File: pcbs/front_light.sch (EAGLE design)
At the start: 13 parts, among them IC1 MC34063AD, J1 22-27-2041-04

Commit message: Front light: use attiny and LT3474
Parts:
- removed D2: SFH206, opto-trans-siemens:SFH206
- added ANODE1, CATHODE1: TPTP20SQ, testpad:TPTP20SQ
- added C10, C11, C14, C5: 100n, resistor:C-EUC0603
- added C13: 100u, resistor:CPOL-EUE
- added C3, C8: 220n, resistor:C-EUC0603
- added C4, C9: 3.3n, resistor:C-EUC0603
- added C6, C7: 2.2u, resistor:C-EUC0805
- added D3: LL5819, Brunner:DIODESCHOTTKY
- added H1: MOUNT-HOLE3.0, holes:MOUNT-HOLE3.0
- added IC2: LT3474, ltc_swr:LT3474
- added IC3: ATTINY24/44/84-SSU, attiny24_44_84:ATTINY24/44/84-SSU
- added J2: 22-27-2041-04, con-molex:22-27-2041-04
- added L2: DR74, inductors:DR74
- added LED1: (no value), led:LEDCHIPLED_0603
- added LIGHT, SPEED_SENSOR: 22-27-2021-02, con-molex:22-27-2021-02
- added LOGO1: OSHW_LOGO_6MILX0100-NT, ea:OSHW_LOGO_6MILX0100-NT
- added R10: 100k, resistor:R-EU_R0603
- added R11, R5: 10k, resistor:R-EU_R0603
- added R12, R6: 20k, resistor:R-EU_R0603
- added R13, R14: (no value), resistor:R-EU_R0603
- added R7, R8: 52.3k, resistor:R-EU_R0603
- added R9: 33, resistor:R-EU_R0603
- added U$1: TPS71530, ShortCircuitRobotics:TPS71530
- added U$2: ISP_SPECIALS, bookla:ISP_SPECIALS
- added U$4: IRF7103, irf-2:IRF7103
- C1: value 10u -> 2.2u; device resistor:C-EUC1206 -> resistor:C-EUC0805
- C2: value 330p -> 2.2u
- IC1: value MC34063AD -> LT3474; device v-reg-3:MC34063AD -> ltc_swr:LT3474
- J1: value 22-27-2041-04 -> (none); device con-molex:22-27-2041-04 -> con-amp:MTA02-156
- L1: value 470u -> DR74; device inductor-coilcraft:MSS1260 -> inductors:DR74
- R1: value 1R0 -> 52.3k; device rcl:R-EU_R1206 -> resistor:R-EU_R0603
- R2: value (none) -> 52.3k; device resistor:R-EU_R1206 -> resistor:R-EU_R0603
- R3: value 1R0 -> 33; device rcl:R-EU_R1206 -> resistor:R-EU_R0603
- R4: value 1R0 -> 100k; device rcl:R-EU_R1206 -> resistor:R-EU_R0603
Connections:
- removed net LED_A: ANODE.TP, IC1.IPK, R1.2, R3.2, R4.2
- removed net LED_C: CATHODE.TP, L1.P$1
- removed net LIGHT: D2.C, J1-3.S
- removed net PWM: IC1.COMP, J1-2.S, R2.2
- new net +12V: C1.1, C11.1, C13.+, C6.1, IC1G$1.#SHDN, IC1G$1.V_IN, IC2G$1.#SHDN, IC2G$1.V_IN, J1.1, U$1.VIN
- new net DI: IC3.(PCINT6/OC1A/SDA/MOSI/ADC6)PA6, J2-3.S, U$2.MOSI
- new net DO: IC3.(PCINT5/OC1B/MISO/DO/ADC5)PA5, J2-2.S, U$2.MISO
- new net N$10: R3.2, R4.2, U$4G$2.G
- new net N$11: IC1G$1.V_ADJ, R5.1, R6.2
- new net N$12: C8.2, D1.C, IC2G$1.SW, L1.1
- new net N$13: C7.1, IC2G$1.BIAS, IC2G$1.OUT, L1.2
- new net N$14: IC2G$1.RT, R7.2
- new net N$15: IC2G$1.REF, R11.1
- new net N$16: C8.1, IC2G$1.BOOST
- new net N$17: C9.1, IC2G$1.V_C, R8.2
- new net N$18: C10.1, R8.1
- new net N$19: ANODE1.TP, IC2G$1.LED
- new net N$2: C2.1, IC1G$1.BIAS, IC1G$1.OUT, L2.2
- new net N$20: CATHODE1.TP, U$4G$1.D@1, U$4G$1.D@2
- new net N$21: R10.2, R9.2, U$4G$1.G
- new net N$22: IC2G$1.V_ADJ, R11.2, R12.2
- new net N$23: IC3.(PCINT4/T1/SCL/USCK/ADC4)PA4, U$2.SCK
- new net N$24: IC3.(PCINT0/AREF/ADC0)PA0, LIGHT-1.S, R14.1
- new net N$25: IC3.(PCINT3/T0/ADC3)PA3, R13.1
- new net N$26: LED1.A, R13.2
- new net N$27: IC3.(PCINT1/AIN0/ADC1)PA1, SPEED_SENSOR-1.S
- new net N$3: IC1G$1.REF, R5.2
- new net N$4: IC1G$1.RT, R1.2
- new net N$5: C3.1, IC1G$1.BOOST
- new net N$6: C4.1, IC1G$1.V_C, R2.2
- new net N$8: ANODE.TP, IC1G$1.LED
- new net N$9: CATHODE.TP, U$4G$2.D@1, U$4G$2.D@2
- new net PWM_BIG_LED: IC2G$1.PWM, IC3.(PCINT7/ICP/OC0B/ADC7)PA7, R9.1
- new net PWM_DLR: IC1G$1.PWM, IC3.(PCINT10/INT0/OC0A/CKOUT)PB2, R3.1
- new net RESET: IC3.(PCINT11/RESET/DW)PB3, U$2.RESET
- new net WAKE_UP: IC3.(PCINT2/AIN1/ADC2)PA2, J2-1.S
- net GND: now also C10.2, C11.2, C13.-, C14.2, C4.2, C5.2, C6.2, C7.2, C9.2, D1.A, D3.A, IC1G$1.GND, IC2G$1.GND, IC3.GND, J1.2, J2-4.S, LED1.C, LIGHT-2.S, R1.1, R10.1, R12.1, R4.1, R6.1, R7.1, SPEED_SENSOR-2.S, U$1.GND, U$2.GND, U$4G$1.S, U$4G$2.S; no longer D2.A, IC1.GND, IC1.SWE, J1-4.S, R2.1
- net N$1: now also C3.2, D3.C, IC1G$1.SW, L2.1; no longer D1.A, IC1.DRC, IC1.SWC, L1.P$2
- net N$7: now also C5.1, R2.1; no longer C2.1, IC1.TC
- net VCC: now also C14.1, IC3.VCC, R14.2, U$1.VOUT, U$2.VCC; no longer C1.1, D1.C, IC1.VCC, J1-1.S, R1.1, R3.1, R4.1
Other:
- note added: "0.7 MHz Switching Frequency"
- note added: "2/3 * 1A = 667mA"
- note removed: "KSQ_PLED_SMD"

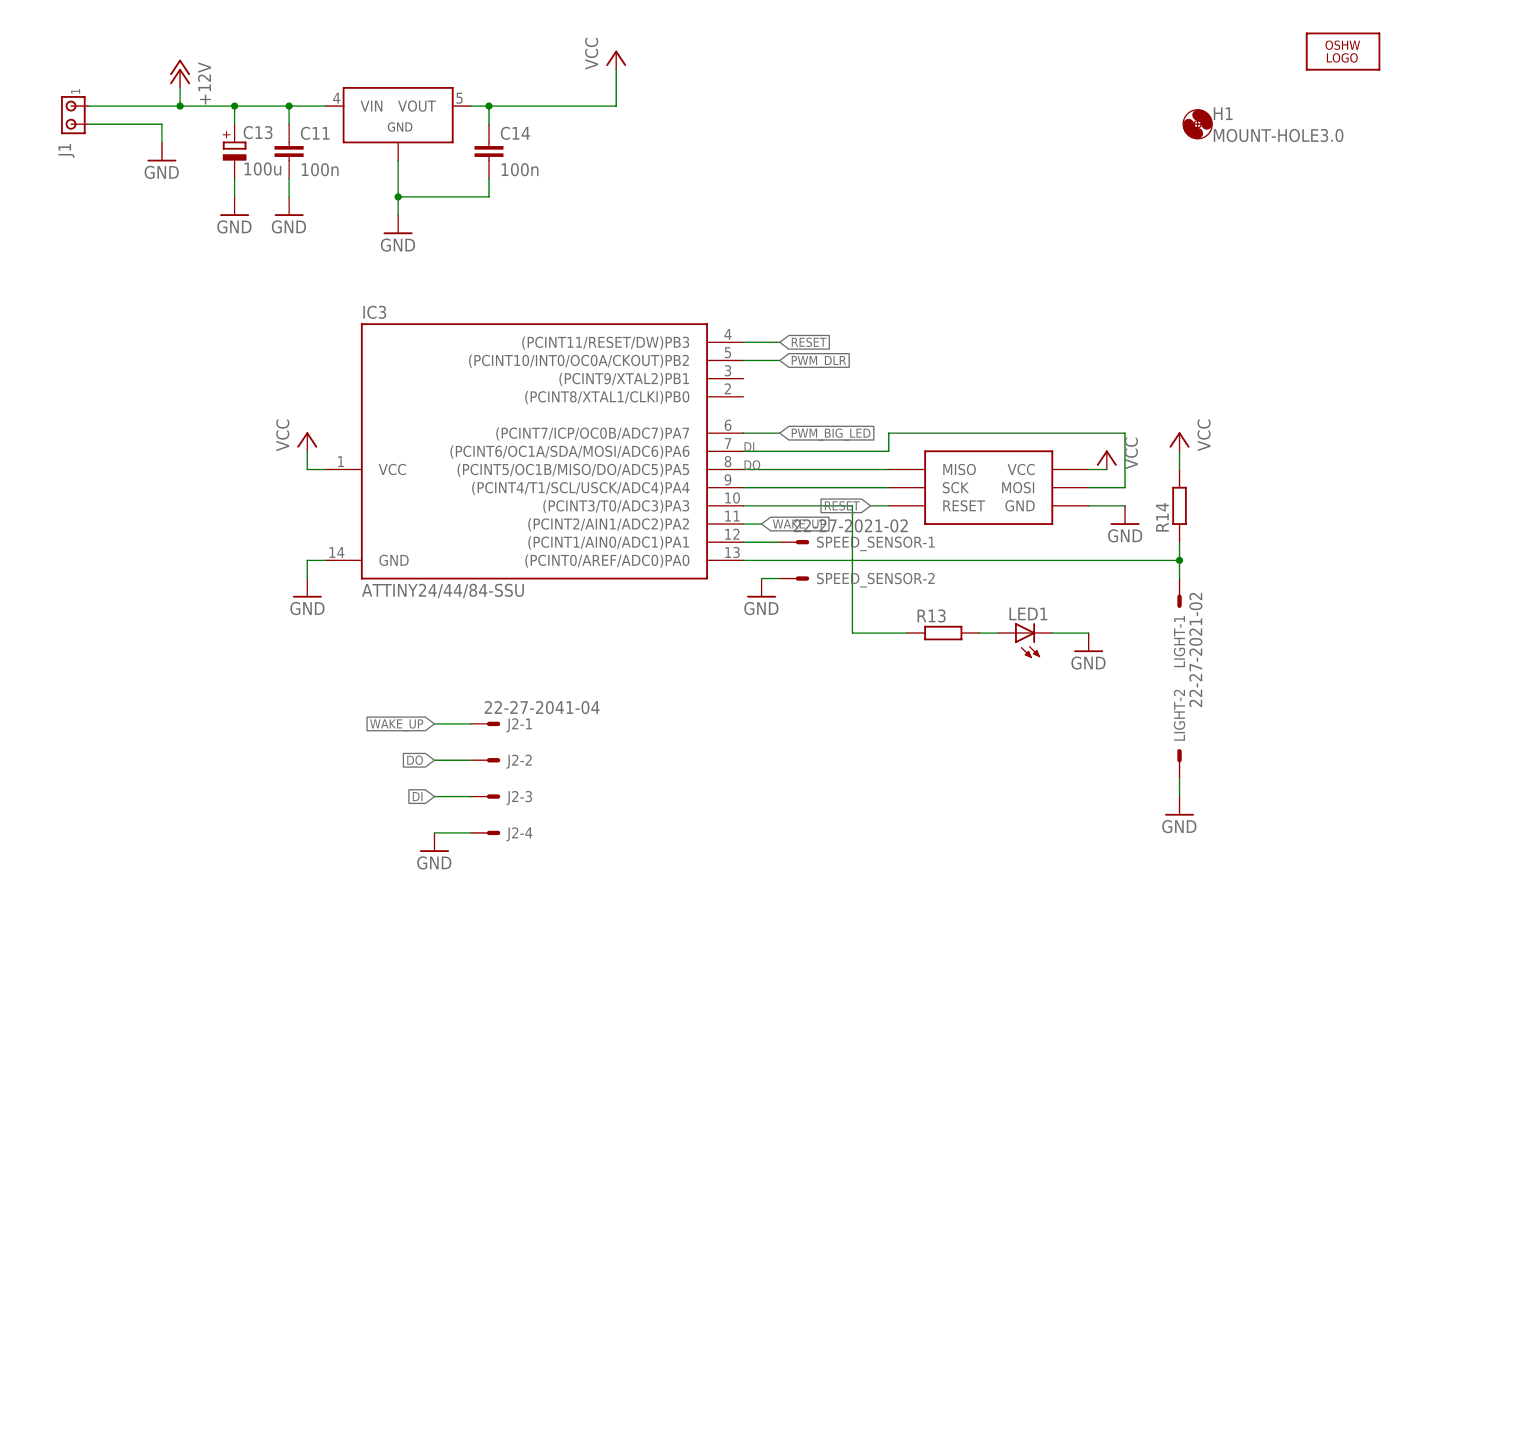
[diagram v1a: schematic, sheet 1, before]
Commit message: ForntLight: improved silkscreen
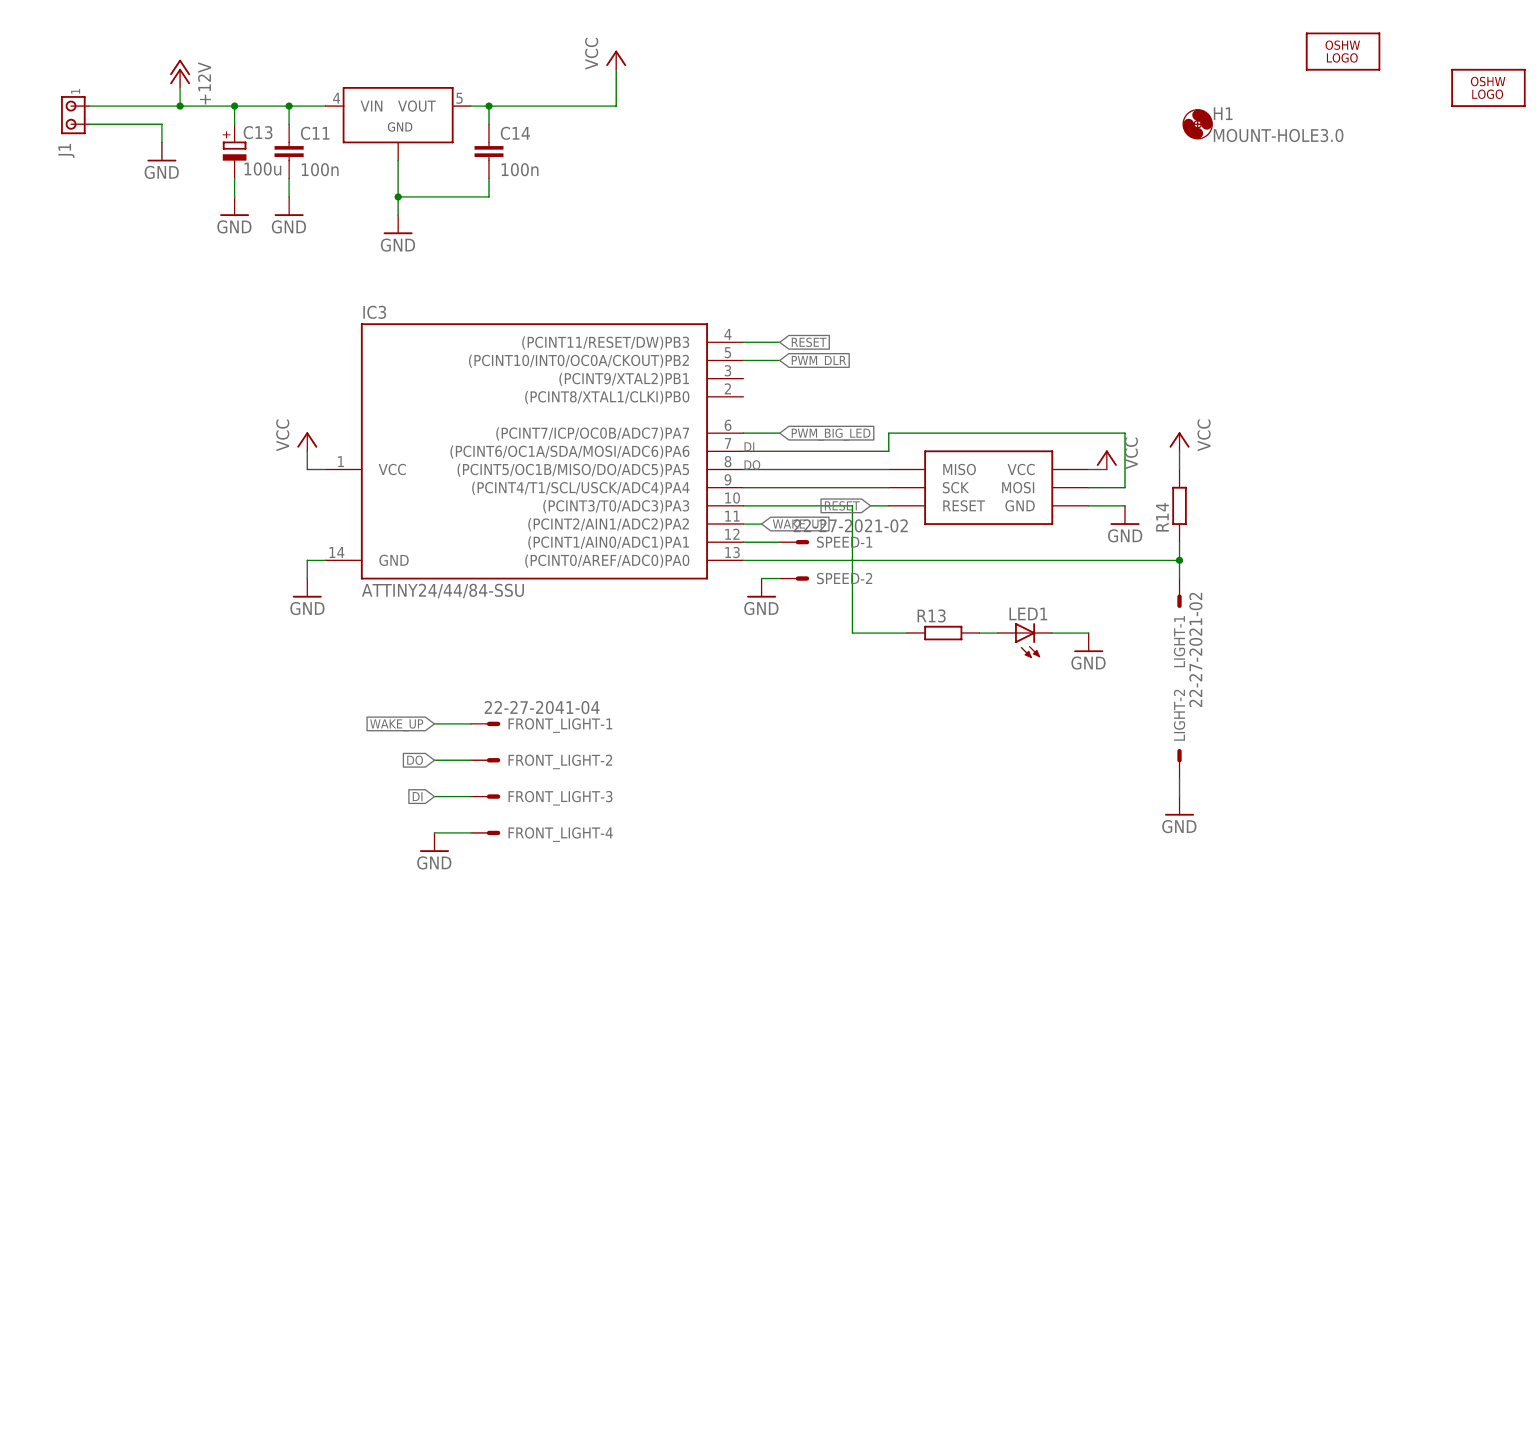
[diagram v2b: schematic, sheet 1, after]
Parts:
- added LOGO2: OSHW_LOGO_10MILX0350-NT, ea:OSHW_LOGO_10MILX0350-NT
- renumbered ANODE to +_D, ANODE1 to +_B, CATHODE to -_D, CATHODE1 to -_B, J2 to FRONT_LIGHT, SPEED_SENSOR to SPEED, U$4 to IRF7103
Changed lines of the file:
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@@
 <part name="GND6" library="supply1" deviceset="GND" device=""/>
 <part name="GND7" library="supply1" deviceset="GND" device=""/>
-<part name="ANODE" library="testpad" deviceset="TP" device="TP20SQ"/>
-<part name="CATHODE" library="testpad" deviceset="TP" device="TP20SQ"/>
-<part name="U$4" library="irf-2" deviceset="IRF7103" device=""/>
+<part name="+_D" library="testpad" deviceset="TP" device="TP20SQ"/>
+<part name="-_D" library="testpad" deviceset="TP" device="TP20SQ"/>
+<part name="IRF7103" library="irf-2" deviceset="IRF7103" device=""/>
 <part name="R3" library="resistor" deviceset="R-EU_" device="R0603" value="33"/>
 <part name="R4" library="resistor" deviceset="R-EU_" device="R0603" value="100k"/>
@@
 <part name="GND15" library="supply1" deviceset="GND" device=""/>
 <part name="GND16" library="supply1" deviceset="GND" device=""/>
-<part name="ANODE1" library="testpad" deviceset="TP" device="TP20SQ"/>
-<part name="CATHODE1" library="testpad" deviceset="TP" device="TP20SQ"/>
+<part name="+_B" library="testpad" deviceset="TP" device="TP20SQ"/>
+<part name="-_B" library="testpad" deviceset="TP" device="TP20SQ"/>
 <part name="R9" library="resistor" deviceset="R-EU_" device="R0603" value="33"/>
 <part name="R10" library="resistor" deviceset="R-EU_" device="R0603" value="100k"/>
@@
 <part name="GND24" library="supply1" deviceset="GND" device=""/>
 <part name="LIGHT" library="con-molex" deviceset="22-?-02" device="27-2021"/>
-<part name="J2" library="con-molex" deviceset="22-?-04" device="27-2041"/>
+<part name="FRONT_LIGHT" library="con-molex" deviceset="22-?-04" device="27-2041"/>
 <part name="GND25" library="supply1" deviceset="GND" device=""/>
 <part name="H1" library="holes" deviceset="MOUNT-HOLE" device="3.0"/>
@@
 <part name="J1" library="con-amp" deviceset="MTA02-156" device=""/>
 <part name="GND27" library="supply1" deviceset="GND" device=""/>
-<part name="SPEED_SENSOR" library="con-molex" deviceset="22-?-02" device="27-2021"/>
+<part name="SPEED" library="con-molex" deviceset="22-?-02" device="27-2021"/>
 <part name="GND28" library="supply1" deviceset="GND" device=""/>
+<part name="LOGO2" library="ea" deviceset="OSHW_LOGO_10MIL" device="X0350-NT"/>
 </parts>
 <sheets>
@@
 <instance part="LIGHT" gate="-1" x="182.88" y="88.9" rot="R270"/>
 <instance part="LIGHT" gate="-2" x="182.88" y="66.04" rot="R90"/>
-<instance part="J2" gate="-1" x="86.36" y="71.12"/>
-<instance part="J2" gate="-2" x="86.36" y="66.04"/>
-<instance part="J2" gate="-3" x="86.36" y="60.96"/>
-<instance part="J2" gate="-4" x="86.36" y="55.88"/>
+<instance part="FRONT_LIGHT" gate="-1" x="86.36" y="71.12"/>
+<instance part="FRONT_LIGHT" gate="-2" x="86.36" y="66.04"/>
+<instance part="FRONT_LIGHT" gate="-3" x="86.36" y="60.96"/>
+<instance part="FRONT_LIGHT" gate="-4" x="86.36" y="55.88"/>
 <instance part="GND25" gate="1" x="78.74" y="53.34"/>
 <instance part="H1" gate="G$1" x="185.42" y="154.94"/>
@@
 <instance part="J1" gate="G$1" x="27.94" y="157.48" rot="MR270"/>
 <instance part="GND27" gate="1" x="40.64" y="149.86"/>
-<instance part="SPEED_SENSOR" gate="-1" x="129.54" y="96.52"/>
-<instance part="SPEED_SENSOR" gate="-2" x="129.54" y="91.44"/>
+<instance part="SPEED" gate="-1" x="129.54" y="96.52"/>
+<instance part="SPEED" gate="-2" x="129.54" y="91.44"/>
 <instance part="GND28" gate="1" x="124.46" y="88.9"/>
+<instance part="LOGO2" gate="G$1" x="226.06" y="160.02"/>
 </instances>
 <busses>
@@
 </segment>
 <segment>
-<pinref part="J2" gate="-4" pin="S"/>
+<pinref part="FRONT_LIGHT" gate="-4" pin="S"/>
 <wire x1="83.82" y1="55.88" x2="78.74" y2="55.88" width="0.1524" layer="91"/>
 <pinref part="GND25" gate="1" pin="GND"/>
@@
 <segment>
 <pinref part="GND28" gate="1" pin="GND"/>
-<pinref part="SPEED_SENSOR" gate="-2" pin="S"/>
+<pinref part="SPEED" gate="-2" pin="S"/>
 <wire x1="124.46" y1="91.44" x2="127" y2="91.44" width="0.1524" layer="91"/>
 </segment>
@@
 </segment>
 <segment>
-<pinref part="J2" gate="-3" pin="S"/>
+<pinref part="FRONT_LIGHT" gate="-3" pin="S"/>
 <wire x1="83.82" y1="60.96" x2="78.74" y2="60.96" width="0.1524" layer="91"/>
 <label x="78.74" y="60.96" size="1.27" layer="95" rot="MR0" xref="yes"/>
@@
 </segment>
 <segment>
-<pinref part="J2" gate="-2" pin="S"/>
+<pinref part="FRONT_LIGHT" gate="-2" pin="S"/>
 <wire x1="83.82" y1="66.04" x2="78.74" y2="66.04" width="0.1524" layer="91"/>
 <label x="78.74" y="66.04" size="1.27" layer="95" rot="MR0" xref="yes"/>
@@
 <net name="WAKE_UP" class="0">
 <segment>
-<pinref part="J2" gate="-1" pin="S"/>
+<pinref part="FRONT_LIGHT" gate="-1" pin="S"/>
 <wire x1="83.82" y1="71.12" x2="78.74" y2="71.12" width="0.1524" layer="91"/>
 <label x="78.74" y="71.12" size="1.27" layer="95" rot="MR0" xref="yes"/>
@@
 <segment>
 <pinref part="IC3" gate="1" pin="(PCINT1/AIN0/ADC1)PA1"/>
-<pinref part="SPEED_SENSOR" gate="-1" pin="S"/>
+<pinref part="SPEED" gate="-1" pin="S"/>
 <wire x1="127" y1="96.52" x2="121.92" y2="96.52" width="0.1524" layer="91"/>
 </segment>
@@
 <instance part="GND6" gate="1" x="71.12" y="71.12"/>
 <instance part="GND7" gate="1" x="55.88" y="71.12"/>
-<instance part="ANODE" gate="G$1" x="106.68" y="83.82" rot="R270"/>
-<instance part="CATHODE" gate="G$1" x="106.68" y="66.04"/>
-<instance part="U$4" gate="G$2" x="109.22" y="55.88" rot="MR0"/>
+<instance part="+_D" gate="G$1" x="106.68" y="83.82" rot="R270"/>
+<instance part="-_D" gate="G$1" x="106.68" y="66.04"/>
+<instance part="IRF7103" gate="G$2" x="109.22" y="55.88" rot="MR0"/>
 <instance part="R3" gate="G$1" x="121.92" y="53.34" rot="MR0"/>
 <instance part="R4" gate="G$1" x="114.3" y="48.26" rot="MR90"/>
@@
 <instance part="GND15" gate="1" x="185.42" y="73.66"/>
 <instance part="GND16" gate="1" x="170.18" y="73.66"/>
-<instance part="ANODE1" gate="G$1" x="220.98" y="86.36" rot="R270"/>
-<instance part="CATHODE1" gate="G$1" x="220.98" y="68.58"/>
+<instance part="+_B" gate="G$1" x="220.98" y="86.36" rot="R270"/>
+<instance part="-_B" gate="G$1" x="220.98" y="68.58"/>
 <instance part="R9" gate="G$1" x="236.22" y="55.88" rot="MR0"/>
 <instance part="R10" gate="G$1" x="228.6" y="50.8" rot="MR90"/>
@@
 <instance part="R12" gate="G$1" x="162.56" y="86.36" rot="MR90"/>
 <instance part="GND18" gate="1" x="162.56" y="73.66"/>
-<instance part="U$4" gate="G$1" x="223.52" y="58.42" rot="MR0"/>
+<instance part="IRF7103" gate="G$1" x="223.52" y="58.42" rot="MR0"/>
 </instances>
 <busses>
@@
 </segment>
 <segment>
-<pinref part="U$4" gate="G$2" pin="S"/>
+<pinref part="IRF7103" gate="G$2" pin="S"/>
 <wire x1="106.68" y1="50.8" x2="106.68" y2="40.64" width="0.1524" layer="91"/>
 <wire x1="106.68" y1="40.64" x2="114.3" y2="40.64" width="0.1524" layer="91"/>
@@
 <junction x="220.98" y="43.18"/>
 <pinref part="GND17" gate="1" pin="GND"/>
-<pinref part="U$4" gate="G$1" pin="S"/>
+<pinref part="IRF7103" gate="G$1" pin="S"/>
 </segment>
 <segment>
@@
 <segment>
 <pinref part="IC1" gate="G$1" pin="LED"/>
-<pinref part="ANODE" gate="G$1" pin="TP"/>
+<pinref part="+_D" gate="G$1" pin="TP"/>
 </segment>
 </net>
 <net name="N$9" class="0">
 <segment>
-<pinref part="U$4" gate="G$2" pin="D@1"/>
-<pinref part="U$4" gate="G$2" pin="D@2"/>
+<pinref part="IRF7103" gate="G$2" pin="D@1"/>
+<pinref part="IRF7103" gate="G$2" pin="D@2"/>
 <wire x1="106.68" y1="60.96" x2="104.14" y2="60.96" width="0.1524" layer="91"/>
-<pinref part="CATHODE" gate="G$1" pin="TP"/>
+<pinref part="-_D" gate="G$1" pin="TP"/>
 <wire x1="106.68" y1="60.96" x2="106.68" y2="63.5" width="0.1524" layer="91"/>
 <junction x="106.68" y="60.96"/>
@@
 <net name="N$10" class="0">
 <segment>
-<pinref part="U$4" gate="G$2" pin="G"/>
+<pinref part="IRF7103" gate="G$2" pin="G"/>
 <pinref part="R4" gate="G$1" pin="2"/>
 <pinref part="R3" gate="G$1" pin="2"/>
@@
 <segment>
 <pinref part="IC2" gate="G$1" pin="LED"/>
-<pinref part="ANODE1" gate="G$1" pin="TP"/>
+<pinref part="+_B" gate="G$1" pin="TP"/>
 </segment>
 </net>
@@
 <segment>
 <wire x1="220.98" y1="63.5" x2="218.44" y2="63.5" width="0.1524" layer="91"/>
-<pinref part="CATHODE1" gate="G$1" pin="TP"/>
+<pinref part="-_B" gate="G$1" pin="TP"/>
 <wire x1="220.98" y1="63.5" x2="220.98" y2="66.04" width="0.1524" layer="91"/>
-<pinref part="U$4" gate="G$1" pin="D@1"/>
+<pinref part="IRF7103" gate="G$1" pin="D@1"/>
 <junction x="220.98" y="63.5"/>
-<pinref part="U$4" gate="G$1" pin="D@2"/>
+<pinref part="IRF7103" gate="G$1" pin="D@2"/>
 </segment>
 </net>
@@
 <pinref part="R9" gate="G$1" pin="2"/>
 <wire x1="231.14" y1="55.88" x2="228.6" y2="55.88" width="0.1524" layer="91"/>
-<pinref part="U$4" gate="G$1" pin="G"/>
+<pinref part="IRF7103" gate="G$1" pin="G"/>
 <junction x="228.6" y="55.88"/>
 </segment>
